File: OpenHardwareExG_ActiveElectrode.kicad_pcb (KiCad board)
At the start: 4 copper layers, 19.3 x 19.3 mm, 14 parts, among them K1 CONN_3, P1 CONN_1, U1 LMP7715, U2 LMP7721

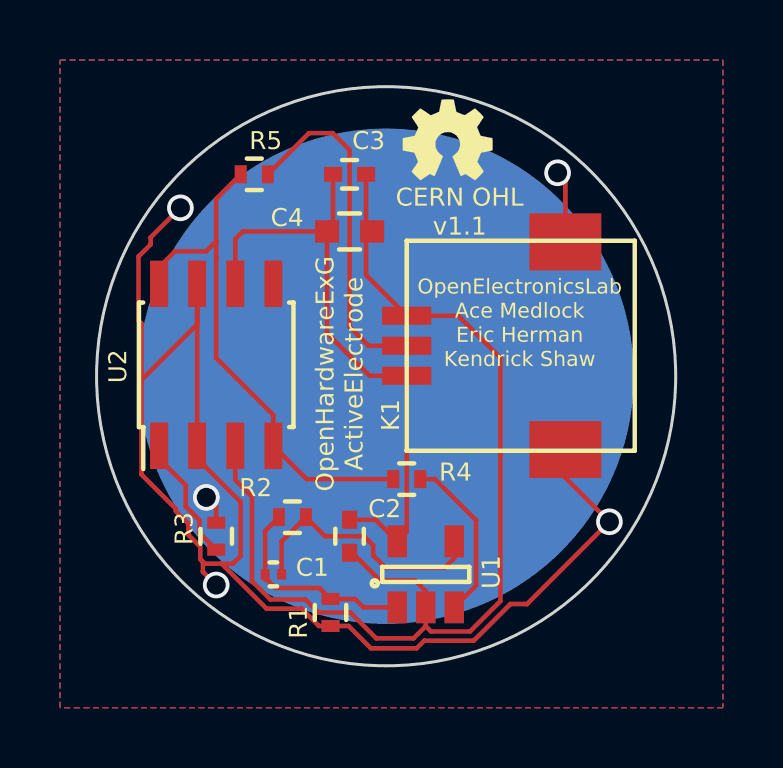
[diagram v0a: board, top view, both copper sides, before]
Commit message: fixed back mask, renamed internal layers for oshpark
Order number dTIGmO2k
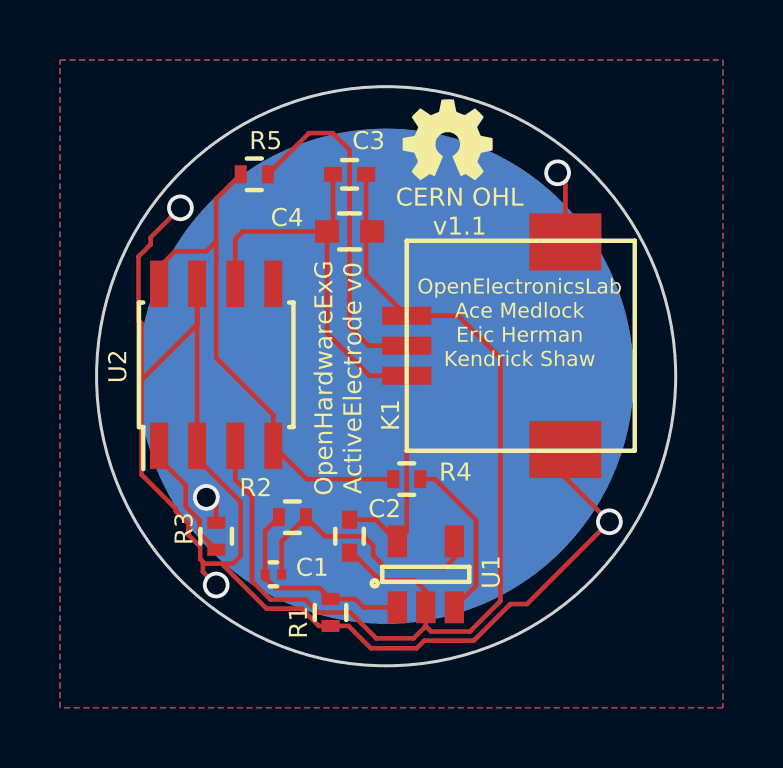
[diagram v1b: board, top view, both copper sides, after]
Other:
- board text added: "OpenHardwareExG ActiveElectrode v0"
- board text removed: "OpenHardwareExG ActiveElectrode"
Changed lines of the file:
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@@
     (links 26)
     (no_connects 0)
-    (area 91.847199 41.478999 111.251201 60.883001)
+    (area 90.678 40.64 112.776001 62.230001)
     (thickness 1.6)
     (drawings 4)
@@
   (layers
     (0 F.Cu signal)
-    (1 In1.Cu signal hide)
-    (2 In2.Cu signal hide)
-    (31 B.Cu signal hide)
-    (33 F.Adhes user)
+    (1 In1.Cu signal)
+    (2 In2.Cu signal)
+    (31 B.Cu signal)
+    (34 B.Paste user)
     (35 F.Paste user)
+    (36 B.SilkS user)
     (37 F.SilkS user)
+    (38 B.Mask user)
     (39 F.Mask user)
-    (40 Dwgs.User user)
-    (41 Cmts.User user)
-    (42 Eco1.User user)
-    (43 Eco2.User user)
     (44 Edge.Cuts user)
     (45 Margin user)
-    (47 F.CrtYd user)
-    (49 F.Fab user)
   )
   (setup
@@
     (trace_clearance 0.1524)
     (zone_clearance 0.254)
-    (zone_45_only no)
+    (zone_45_only yes)
     (trace_min 0.1524)
     (segment_width 0.2)
@@
     (pad_to_mask_clearance 0)
     (aux_axis_origin 0 0)
-    (visible_elements 7FFEFBFF)
+    (visible_elements 7FFEFFFF)
     (pcbplotparams
-      (layerselection 0x010a8_80000007)
+      (layerselection 0x030fc_80000007)
       (usegerberextensions true)
       (excludeedgelayer true)
@@
       (effects (font (size 0.6 0.6) (thickness 0.127)) (justify mirror))
     )
-    (pad 1 smd circle (at -0.0508 0.381) (size 16.51 16.51) (layers B.Cu)
+    (pad 1 smd circle (at -0.0508 0.381) (size 16.51 16.51) (layers B.Cu B.Mask)
       (net 3 /ELECTRODE))
   )
@@
     (effects (font (size 0.5 0.5) (thickness 0.1)))
   )
-  (gr_text "OpenHardwareExG\nActiveElectrode" (at 100 51.1 90) (layer F.SilkS)
+  (gr_text "OpenHardwareExG\nActiveElectrode v0" (at 99.96 51.24 90) (layer F.SilkS)
     (effects (font (size 0.6 0.6) (thickness 0.127)))
   )
@@
   (via (at 95.5548 55.2196) (size 0.889) (drill 0.635) (layers F.Cu B.Cu) (net 3))
   (segment (start 95.885 55.5498) (end 95.5548 55.2196) (width 0.1524) (layer F.Cu) (net 3))
+  (segment (start 107.525 44.66) (end 107.2642 44.3992) (width 0.1524) (layer F.Cu) (net 4))
+  (via (at 107.2642 44.3992) (size 0.889) (drill 0.635) (layers F.Cu B.Cu) (net 4))
+  (segment (start 107.525 46.705) (end 107.525 44.66) (width 0.1524) (layer F.Cu) (net 4))
+  (via (at 108.9914 56.0324) (size 0.889) (drill 0.635) (layers F.Cu B.Cu) (net 4))
   (segment (start 99.695 59.505) (end 100.2974 59.505) (width 0.1524) (layer F.Cu) (net 4))
-  (via (at 108.9914 56.0324) (size 0.889) (drill 0.635) (layers F.Cu B.Cu) (net 4))
   (segment (start 108.9914 56.0324) (end 107.525 54.566) (width 0.1524) (layer F.Cu) (net 4))
   (segment (start 106.2482 58.7756) (end 108.9914 56.0324) (width 0.1524) (layer F.Cu) (net 4))
@@
   (segment (start 100.2974 59.505) (end 101.0412 60.2488) (width 0.1524) (layer F.Cu) (net 4))
   (segment (start 107.525 53.625) (end 107.525 54.566) (width 0.1524) (layer F.Cu) (net 4))
-  (segment (start 107.525 46.705) (end 107.525 44.66) (width 0.1524) (layer F.Cu) (net 4))
-  (via (at 107.2642 44.3992) (size 0.889) (drill 0.635) (layers F.Cu B.Cu) (net 4))
-  (segment (start 107.525 44.66) (end 107.2642 44.3992) (width 0.1524) (layer F.Cu) (net 4))
   (segment (start 93.3958 51.308) (end 93.3958 49.4284) (width 0.1524) (layer F.Cu) (net 4))
   (via (at 94.6912 45.5676) (size 0.889) (drill 0.635) (layers F.Cu B.Cu) (net 4))
@@
     (polygon
       (pts
-        (xy 90.678 40.64) (xy 112.776 40.64) (xy 112.776 62.23) (xy 90.678 62.23)
+        (xy 90.678 40.64) (xy 112.776 40.64) (xy 110.77 51.16) (xy 112.776 62.23) (xy 90.678 62.23)
       )
     )
